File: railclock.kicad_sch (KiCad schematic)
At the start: 177 parts, among them J1 Conn_01x02_Pin, J10 Conn_01x04_MountingPin, J11 Conn_01x04_MountingPin, J12 Conn_01x04_MountingPin, J13 Conn_01x04_MountingPin, J14 Conn_01x04_MountingPin, J15 Conn_01x03_MountingPin, J16 Barrel_Jack_Switch, J2 Conn_01x03_MountingPin, J3 Conn_01x04_MountingPin, J4 USB_C_Receptacle_USB2.0_14P, J5 Conn_01x03_MountingPin, J6 Conn_01x03_MountingPin, J7 Conn_01x03_MountingPin, J8 Conn_01x03_MountingPin, J9 Conn_01x04_MountingPin, Q1 Q_NPN_BEC, SW1 SW_SPST, SW2 SW_DPDT_x2, U1 MCP7940N-xST, U10 74AHC1G04, U11 MAX811TEUS-T, U12 MCP4728, U13 BTS5012SDA, U14 BTS5012SDA, U15 BTS5012SDA, U16 BTS5012SDA, U17 BTS5012SDA, U2 MCP73832-2-OT, U4 ESP32-C6-WROOM-1, U5 DRV8870DDA, U6 PAM2421, U8 BQ24296MRGET, U9 PCF8574RGTR, Y2 Crystal_GND3

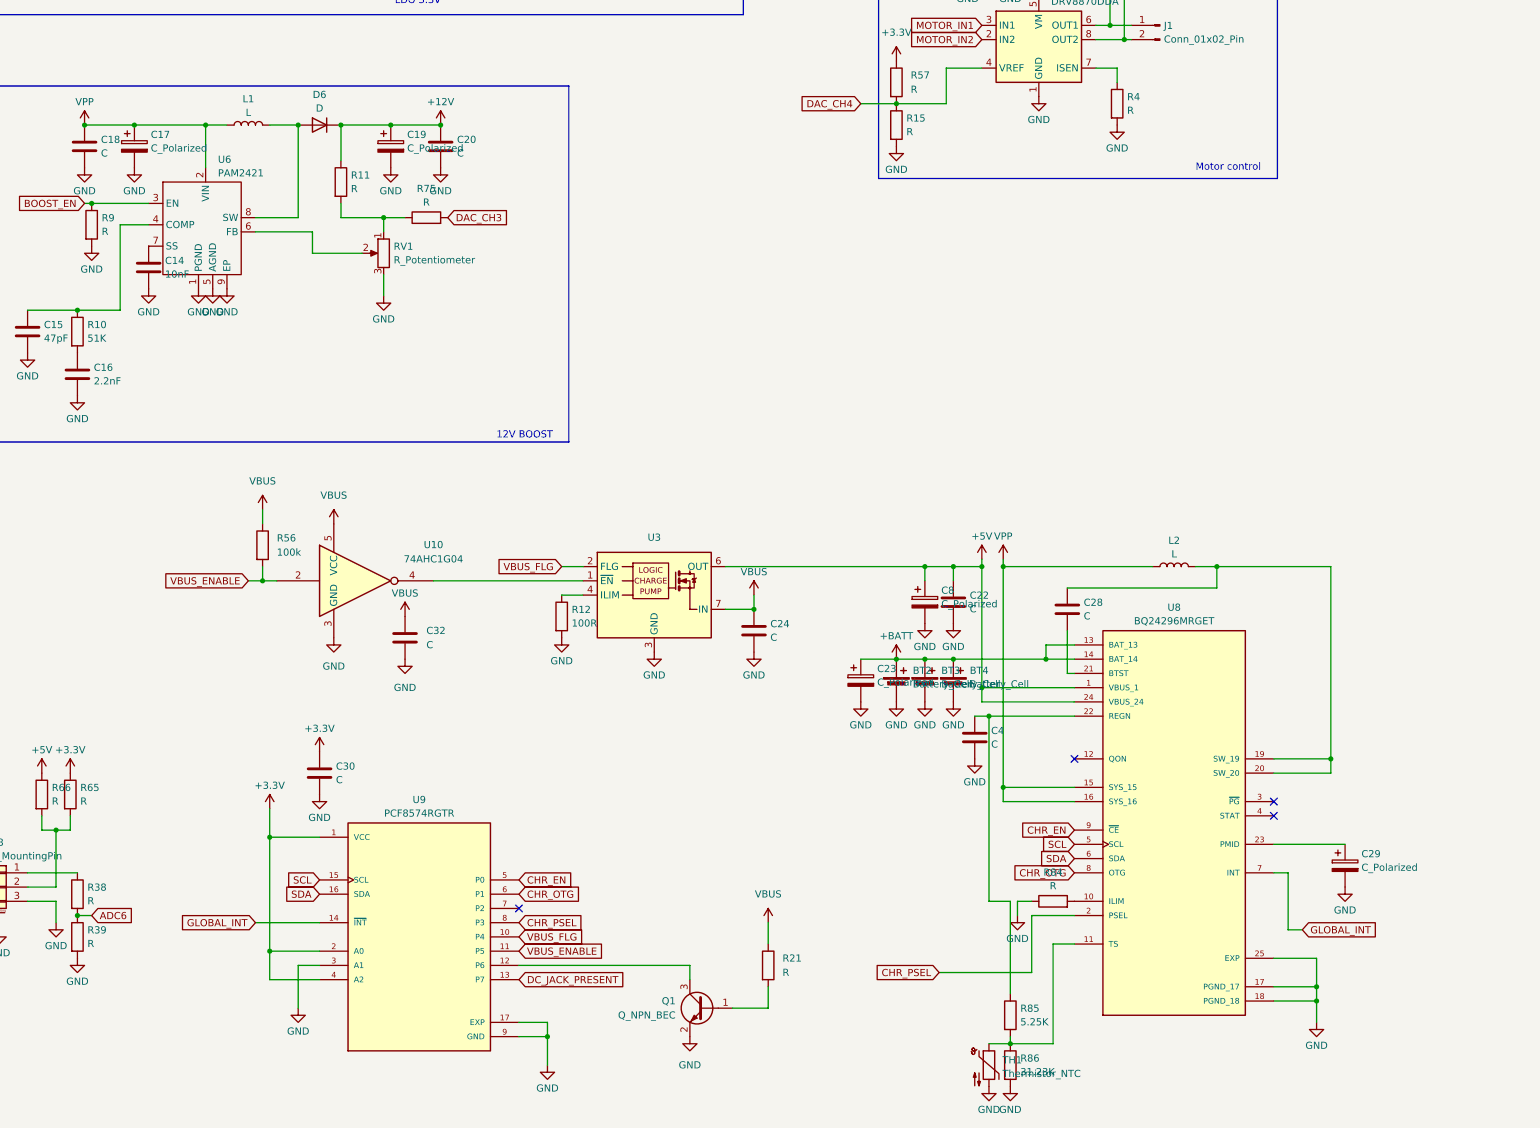
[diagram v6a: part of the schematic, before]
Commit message: Add element values and some fixes
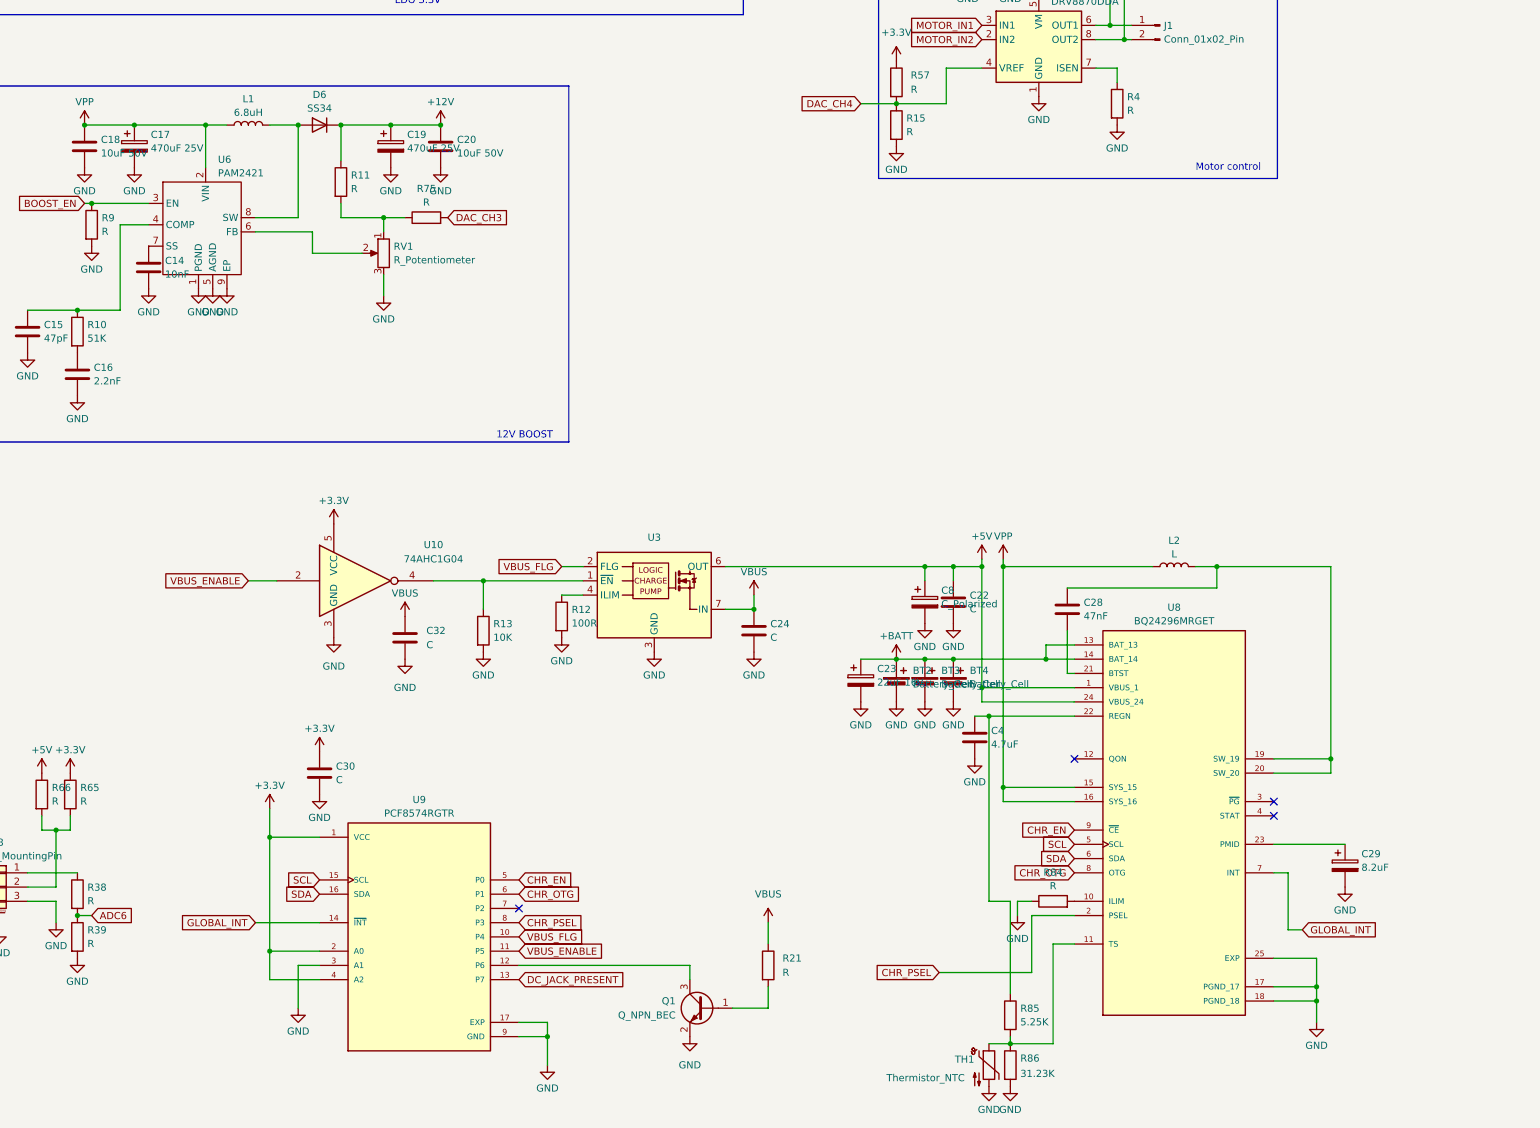
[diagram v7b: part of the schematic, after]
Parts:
- removed R56: 100k, Resistor_SMD:R_0805_2012Metric, symbol Device:R
- added R13: 10K, Resistor_SMD:R_0805_2012Metric, symbol Device:R
- C17, C19: value C_Polarized -> 470uF 25V
- C18, C20: value C -> 10uF 50V; footprint Capacitor_SMD:C_0805_2012Metric -> Capacitor_SMD:C_1210_3225Metric
- C23: value C_Polarized -> 22uF 16V
- C28: value C -> 47nF
- C29: value C_Polarized -> 8.2uF
- C4: value C -> 4.7uF; footprint Capacitor_SMD:C_0805_2012Metric -> Capacitor_SMD:C_1206_3216Metric
- D6: value D -> SS34
- L1: value L -> 6.8uH
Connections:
- net +3.3V: now also U10.5 (VCC)
- net GND: now also R13.2
- net IN: no longer U10.5 (VCC)
- net at U10.4, U3.1 (~{EN}): now also R13.1

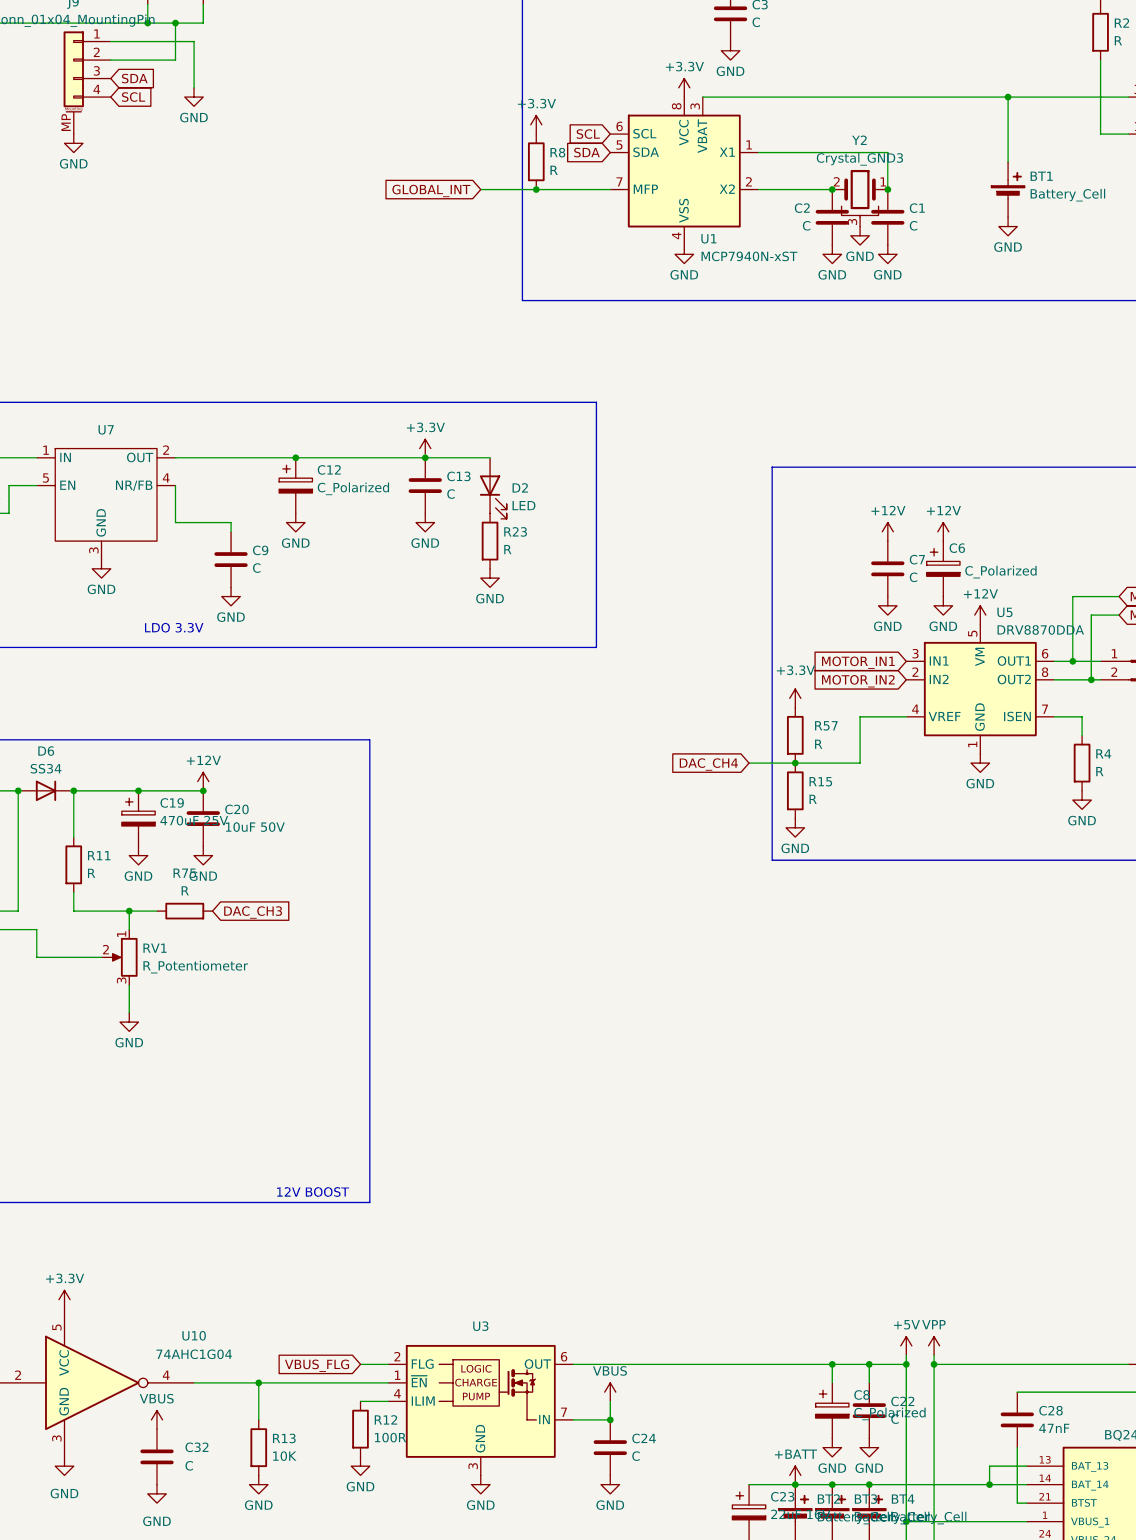
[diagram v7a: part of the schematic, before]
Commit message: Reroute to 4 layer pcb
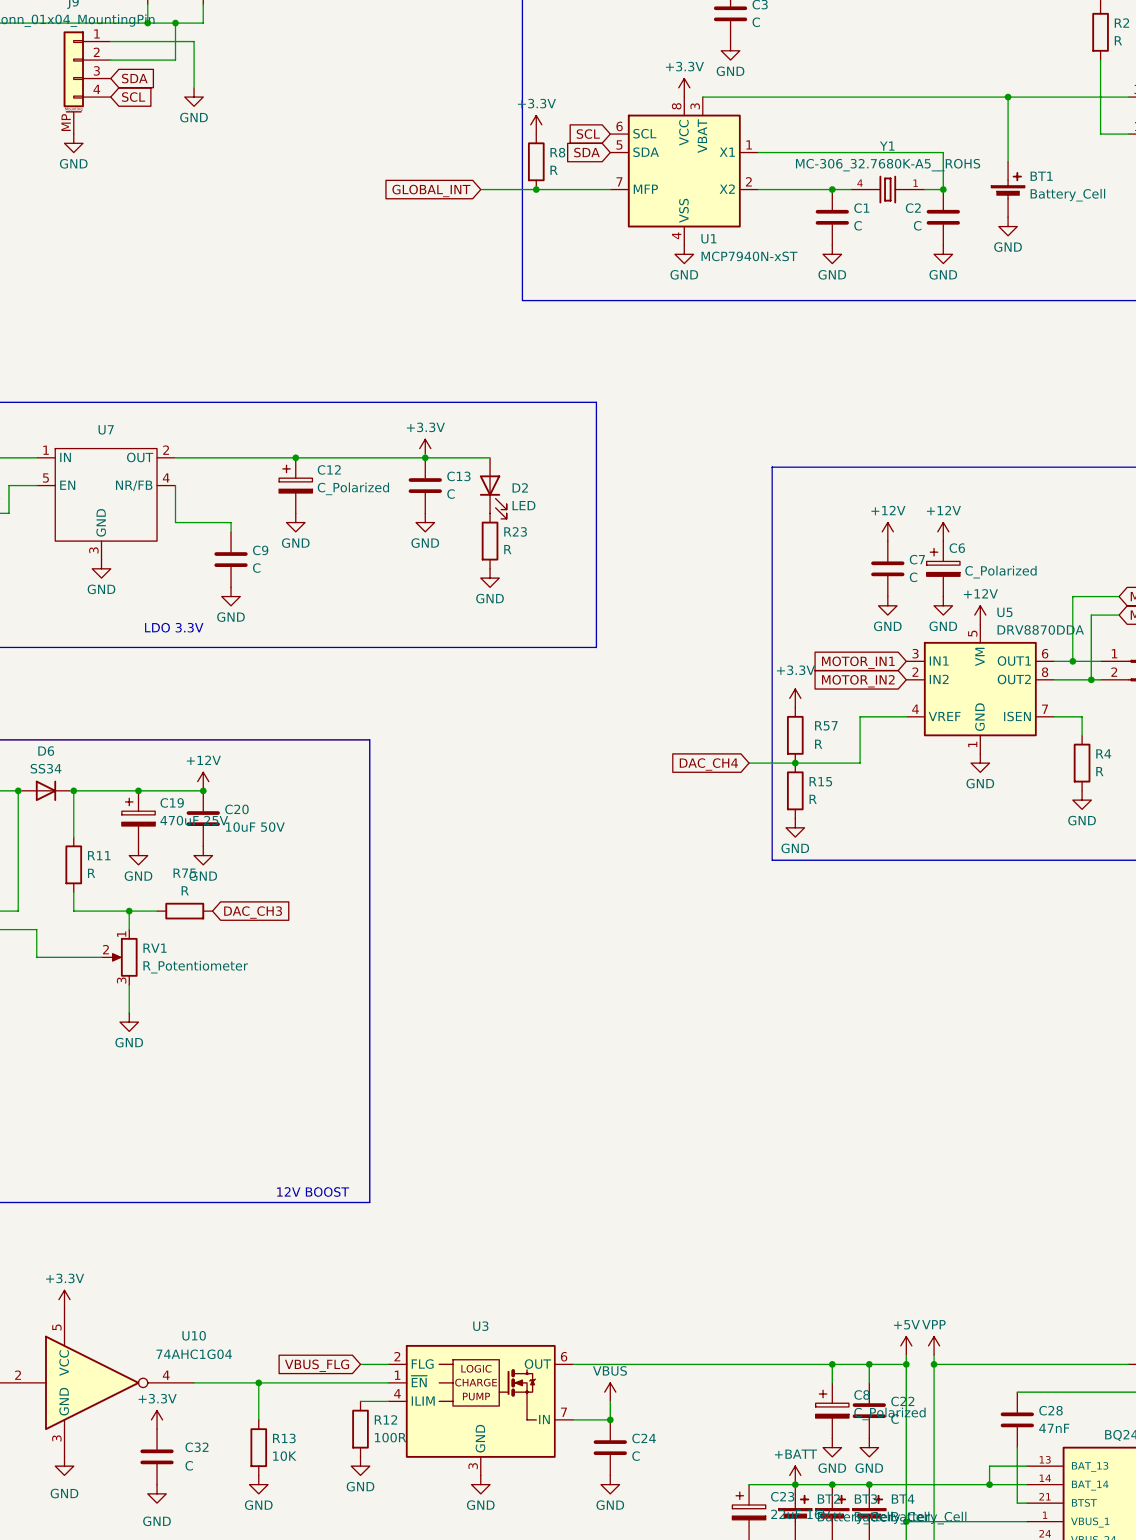
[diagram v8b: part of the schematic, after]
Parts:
- removed Y2: Crystal_GND3, Crystal:Crystal_DS10_D1.0mm_L4.3mm_Horizontal_1EP_style2, symbol Device:Crystal_GND3
- added Y1: MC-306_32.7680K-A5__ROHS, th:OSCL550P800X320X254-4N, symbol MC-306_32.7680K-A5__ROHS:MC-306_32.7680K-A5__ROHS
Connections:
- net +3.3V: now also C32.1
- net IN: no longer C32.1
- net at U1.1 (X1): now also C2.1, Y1.1; no longer C1.1
- net at U1.2 (X2): now also C1.1, Y1.4; no longer C2.1
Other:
- moved on the sheet: C1, C2
